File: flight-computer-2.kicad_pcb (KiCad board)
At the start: 4 copper layers, 51 x 51 mm, 76 parts, among them J1 USB4105-GF-A, J2 THR, J3 SER1, J4 SER2, J5 SER3, J6 SER4, J7 Breakout, SW1 RESET, SW2 BOOT, U1 AP2114H-3.3TRG1, U2 MUN5214DW1T1G, U3 BNO080, U4 CP2102N, U5 MPL3115A2, U6 ESP32-PICO-D4, Y1 32.768kHz

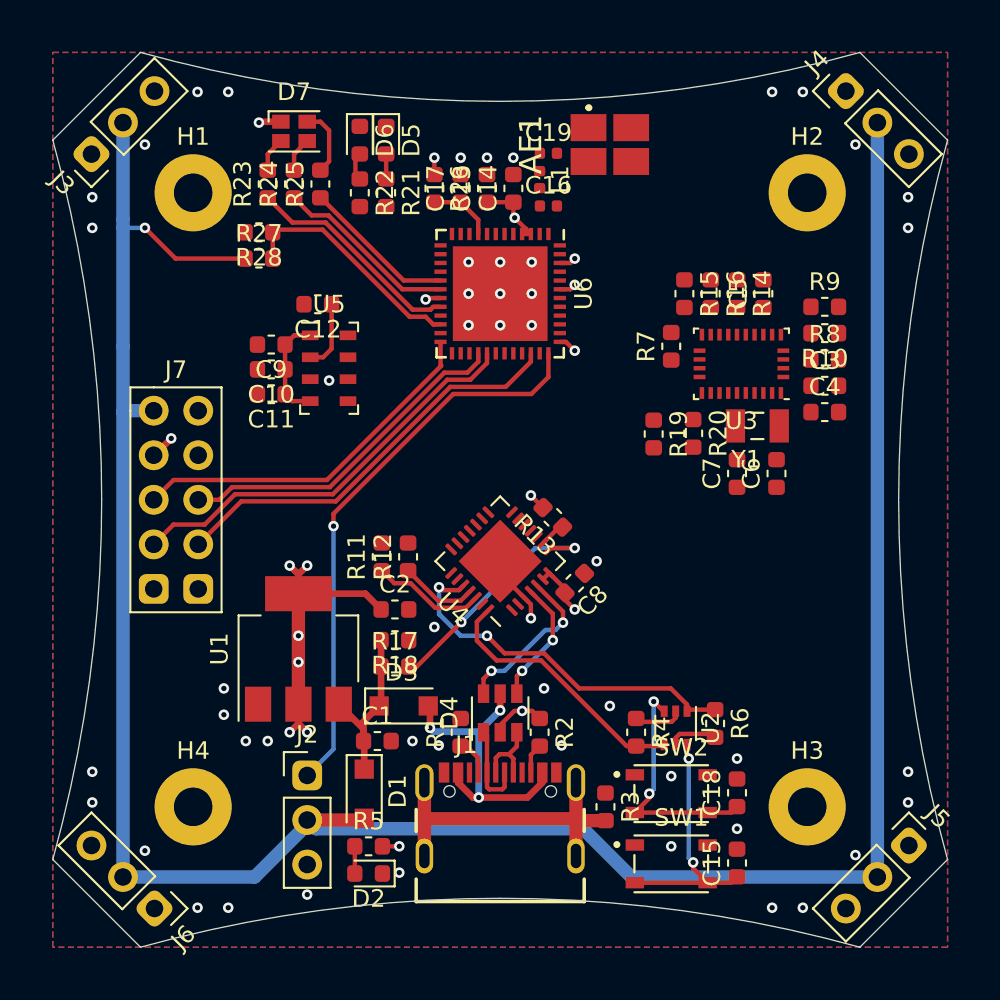
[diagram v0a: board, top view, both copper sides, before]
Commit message: I2C and other crucial signals routed
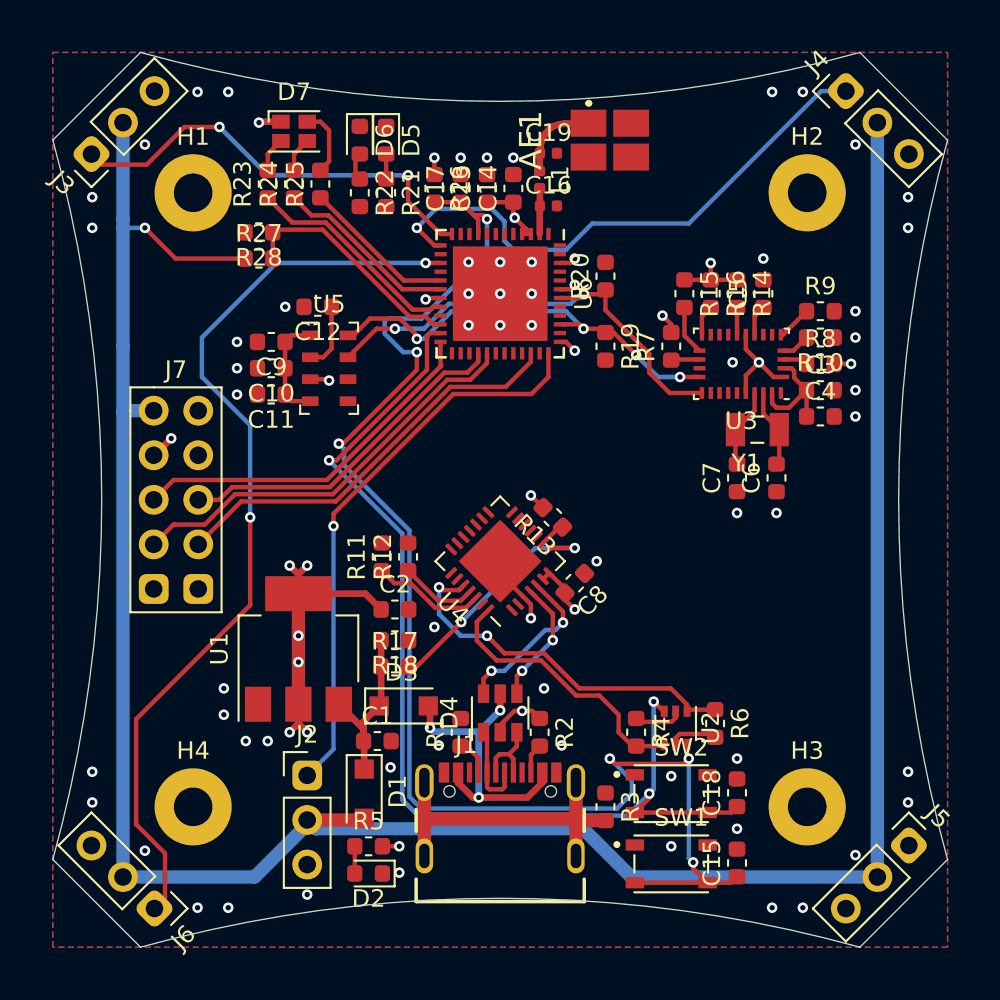
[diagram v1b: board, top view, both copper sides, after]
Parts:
- moved R20 10.3 mm to (123.5, 54.8), turned to 90 degrees
- moved R19 5.71 mm to (123.5, 58.8)
- moved C3 0.35 mm to (135.8, 61.2)
- moved C4 0.35 mm to (135.8, 62.8)
- moved R10 0.35 mm to (135.8, 58.2)
- moved R8 0.35 mm to (135.8, 59.8)
- moved R9 0.35 mm to (135.8, 56.8)
- moved AE1 0.25 mm to (123.8, 47.0)
- moved C6 0.25 mm to (133.2, 66.2)
- moved C7 0.25 mm to (131.0, 66.2)
- moved Y1 0.21 mm to (132.2, 63.5)
- moved C9 0.15 mm to (104.5, 58.5)
- moved C12 0.15 mm to (107.1, 56.5)
- moved C10 0.07 mm to (104.5, 60.0)
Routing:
- net /EN: track 18.1 -> 81.6 mm, vias 2 -> 6
- net /SER4: track 0.00 -> 52.7 mm, vias 0 -> 2
- net /IO0: track 13.6 -> 60.1 mm, vias 2 -> 3
- net /SER2: track 0.00 -> 32.0 mm, vias 0 -> 1
- net /SDA: track 0.00 -> 27.0 mm, vias 0 -> 2
- net /SER1: track 0.00 -> 25.1 mm, vias 0 -> 2
- net /SCL: track 0.00 -> 24.7 mm, vias 0 -> 4
- net +3V3: track 40.1 -> 52.9 mm, vias 17 -> 20
- net GND: track 7.15 -> 13.9 mm, vias 52 -> 64
- net Net-(AE1-Pad1): track 0.00 -> 4.83 mm
- net Net-(C7-Pad2): track 0.00 -> 4.54 mm
- net Net-(C6-Pad2): track 0.00 -> 4.49 mm
- net Net-(R15-Pad2): track 0.00 -> 2.82 mm
- net Net-(C16-Pad1): track 0.00 -> 2.63 mm
- net Net-(R9-Pad1): track 0.00 -> 2.02 mm
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
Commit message: Refactoring pin mapping
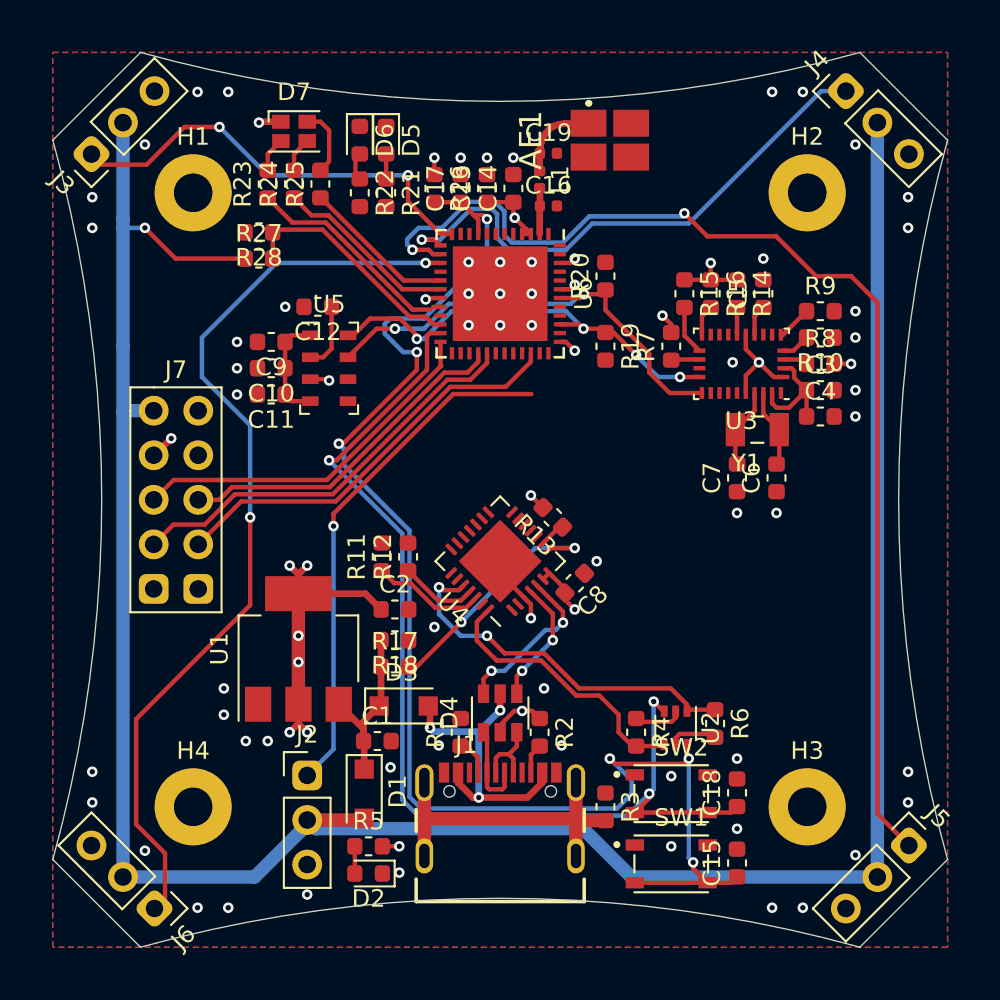
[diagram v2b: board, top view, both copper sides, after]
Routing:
- net /SER3: track 0.00 -> 66.4 mm, vias 0 -> 2
- net /THR: track 32.4 -> 29.6 mm

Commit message: Rerouting progress
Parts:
- D5: value LTST-C191KRKT -> Red
- D6: value LTST-C191TBKT -> Blue
- moved C11 29.8 mm to (131.0, 75.0), turned to 270 degrees
- moved C10 29.2 mm to (129.5, 75.0), turned to 270 degrees
- moved C9 28.8 mm to (128.0, 75.0), turned to 270 degrees
- moved U5 24.7 mm to (129.5, 71.7), turned to 90 degrees
- moved C12 24.7 mm to (126.0, 72.4), turned to 270 degrees
- moved R21 1.52 mm to (109.5, 49.8)
- moved R22 1.52 mm to (111.0, 49.8)
- moved D5 0.25 mm to (111.0, 46.8)
- moved D6 0.25 mm to (109.5, 46.8)
- moved R19 0.25 mm to (123.8, 58.8)
- moved R20 0.25 mm to (123.8, 54.8)
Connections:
- R21 pad 1: Net-(D5-Pad2) -> Net-(D6-Pad2)
- R22 pad 1: Net-(D6-Pad2) -> Net-(D5-Pad2)
- U5 pad 5: /ALT_INT_2 -> (no net)
- U5 pad 6: /ALT_INT_1 -> (no net)
- U6 pad 10: /ALT_INT_1 -> (no net)
- U6 pad 11: /ALT_INT_2 -> (no net)
- U6 pad 12: /SER1 -> Net-(R22-Pad2)
- U6 pad 13: /SER2 -> Net-(R21-Pad2)
- U6 pad 14: /SER3 -> /SER1
- U6 pad 15: /SER4 -> /SER2
- U6 pad 16: /IMU_INT -> /SER4
- U6 pad 35: Net-(R22-Pad2) -> /THR
- U6 pad 36: /THR -> /SER3
- U6 pad 38: Net-(R21-Pad2) -> /IMU_INT
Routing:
- net /SER3: track 66.4 -> 0.00 mm, vias 2 -> 0
- net /SER2: track 31.6 -> 0.00 mm, vias 1 -> 0
- net /SER1: track 25.1 -> 0.00 mm, vias 2 -> 0
- net /TXD0: track 0.00 -> 21.9 mm, vias 0 -> 2
- net /RXD0: track 0.00 -> 21.7 mm, vias 0 -> 2
- net /IMU_INT: track 0.00 -> 10.3 mm, vias 0 -> 2
- net /SER4: track 52.7 -> 45.6 mm, vias 2 -> 4
- net /SDA: track 27.0 -> 21.1 mm
- net /SCL: track 24.7 -> 20.6 mm, vias 4 -> 0
- net /EN: track 81.2 -> 77.2 mm
- net +3V3: track 52.9 -> 55.4 mm, vias 20 -> 22
- net /THR: track 29.6 -> 31.5 mm
- net Net-(D6-Pad2): track 1.42 -> 0.00 mm
- net Net-(D5-Pad2): track 1.42 -> 0.00 mm
- net /IO0: track 60.1 -> 61.0 mm

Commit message: Final draft of routing complete
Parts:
- moved C2 11.0 mm to (103.5, 81.2), turned to 180 degrees
- moved R1 0.25 mm to (115.0, 80.8)
- moved R2 0.25 mm to (120.0, 80.8)
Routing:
- net /SER3: track 0.00 -> 39.0 mm, vias 0 -> 2
- net /SER2: track 0.00 -> 33.6 mm, vias 0 -> 1
- net /SDA: track 21.1 -> 50.2 mm
- net /SCL: track 20.6 -> 47.5 mm, vias 0 -> 1
- net /SER1: track 0.00 -> 23.6 mm, vias 0 -> 2
- net Net-(R21-Pad2): track 0.00 -> 5.62 mm
- net Net-(R22-Pad2): track 0.00 -> 4.50 mm
- net GND: track 13.9 -> 17.7 mm, vias 64 -> 86
- net +3V3: track 55.4 -> 52.1 mm, vias 22 -> 23
- net Net-(D6-Pad2): track 0.00 -> 1.42 mm
- net Net-(D5-Pad2): track 0.00 -> 1.42 mm
- net /VIN: track 10.6 -> 9.84 mm

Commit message: Small adjustments and IC silkscreen
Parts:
- moved D5 0.56 mm to (111.5, 47.0)
- moved D6 0.56 mm to (110.0, 47.0)
- moved R21 0.56 mm to (110.0, 50.0)
- moved R22 0.56 mm to (111.5, 50.0)
- moved AE1 0.25 mm to (123.8, 47.2)
- moved C16 0.25 mm to (120.2, 51.0)
- moved C19 0.25 mm to (120.2, 48.0)
- moved L1 0.25 mm to (119.8, 49.5)
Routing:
- net /SER3: track 39.0 -> 39.5 mm
- net GND: vias 86 -> 79

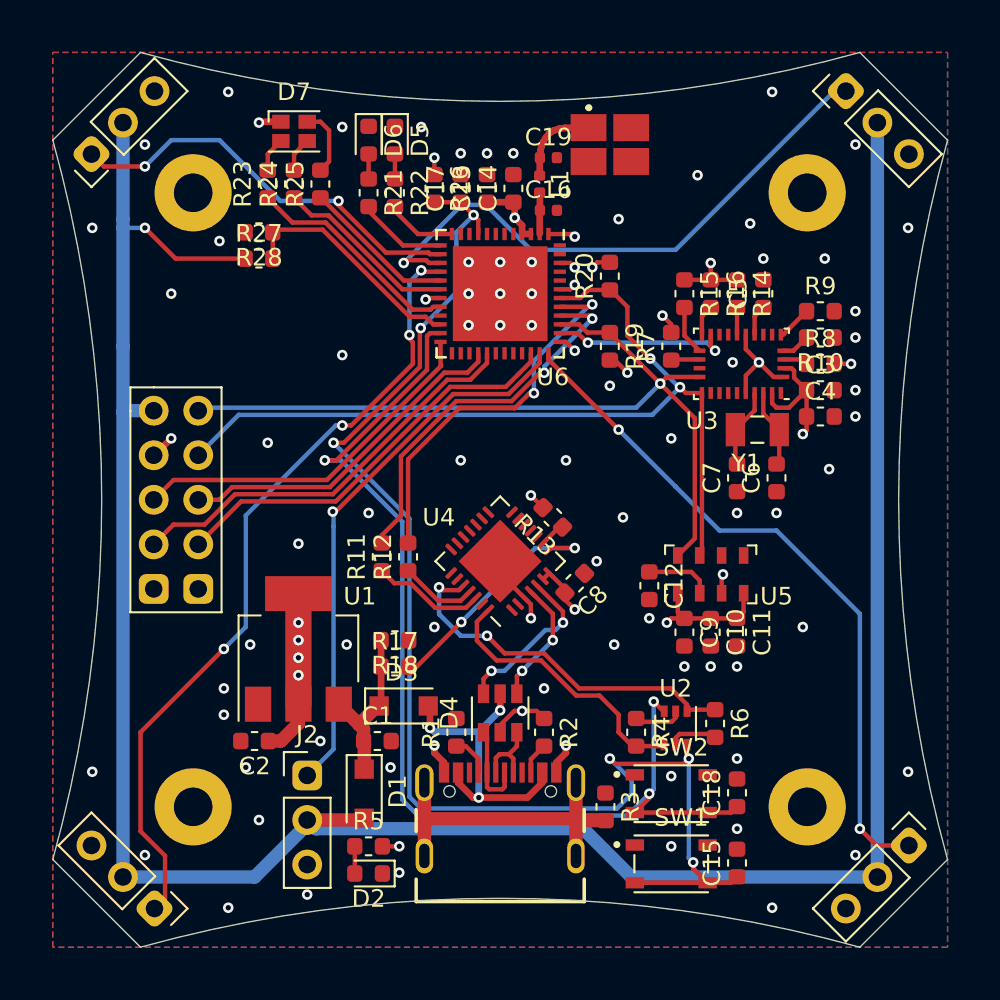
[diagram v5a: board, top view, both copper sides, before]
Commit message: VBEC power filtering cap
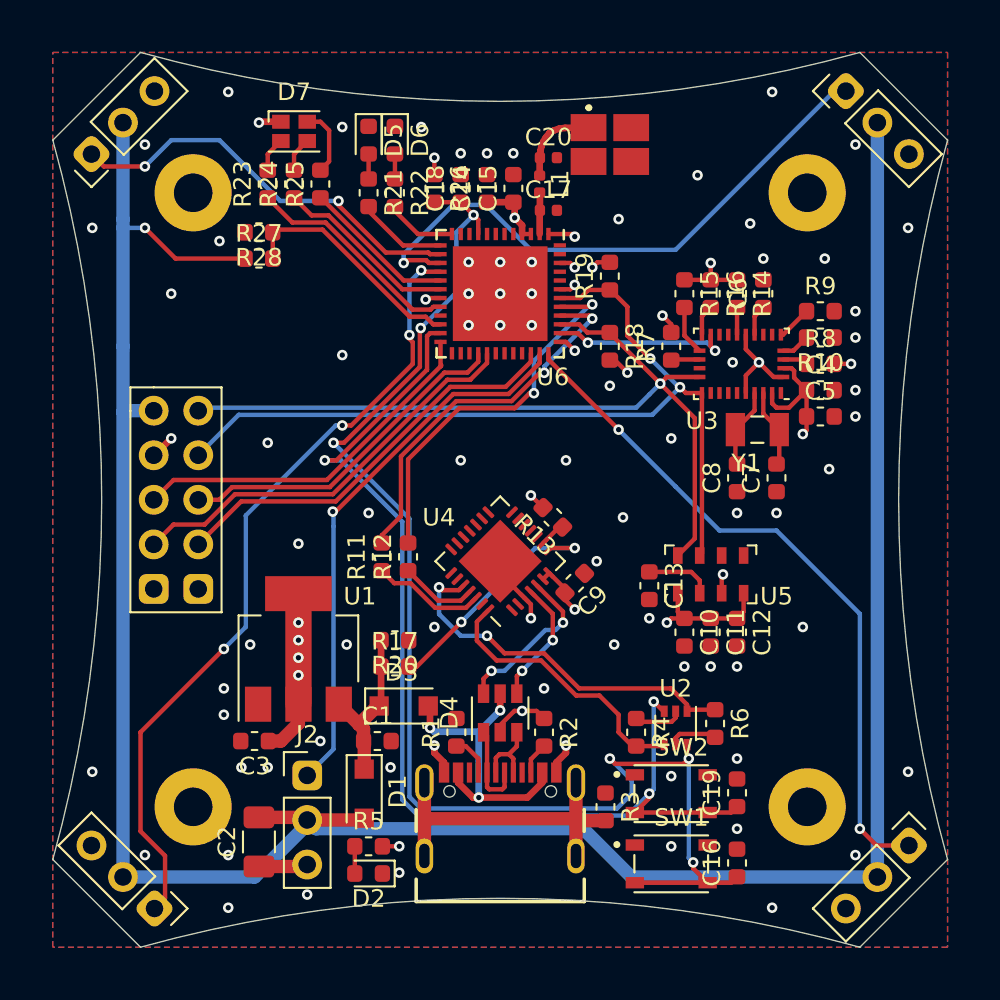
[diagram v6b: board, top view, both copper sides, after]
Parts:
- added C2: 220uF, Capacitor_SMD:C_1206_3216Metric, F.Cu at (103.8, 87.0)
- renumbered C9 to C10, C10 to C11, C11 to C12, C12 to C13, C13 to C14, C14 to C15, C15 to C16, C16 to C17, C17 to C18, C18 to C19, C19 to C20, C2 to C3, C3 to C4, C4 to C5, C5 to C6, C6 to C7, C7 to C8, C8 to C9, D6 to D5, D5 to D6, R19 to R18, R20 to R19, R18 to R20
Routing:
- net /VBEC: track 145.0 -> 147.8 mm
- net GND: track 17.7 -> 20.5 mm, vias 79 -> 80

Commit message: Fixed reference silkscreen
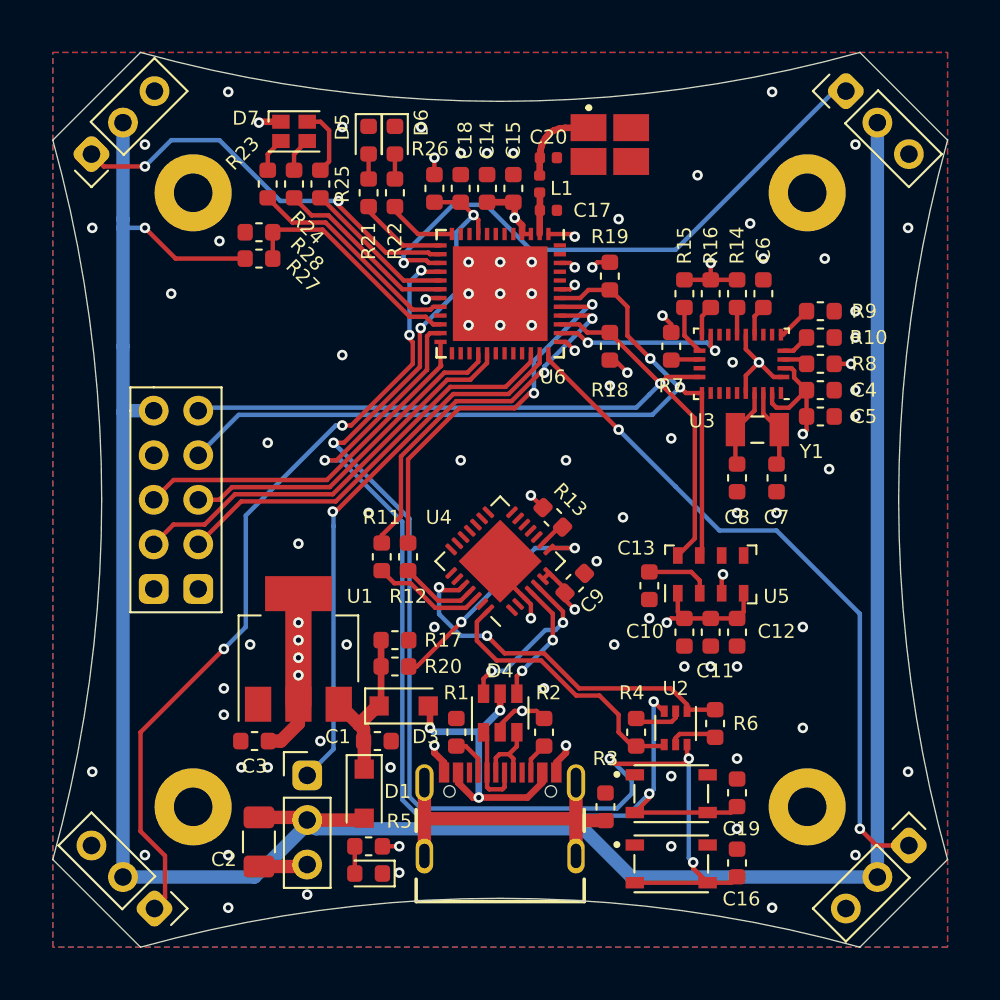
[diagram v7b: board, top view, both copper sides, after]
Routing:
- net +3V3: track 52.2 -> 50.9 mm, vias 23 -> 22
- net GND: vias 80 -> 81

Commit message: Finished top silkscreen and enabled bottom layers
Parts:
- added G***: LOGO, flight-computer-2:cj, F.Cu at (110.6, 65.4)
- added G***: LOGO, flight-computer-2:abacus, F.Cu at (110.8, 63.0)
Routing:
- net +3V3: vias 22 -> 23
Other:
- board text added: "RST"
- board text added: "V1"
